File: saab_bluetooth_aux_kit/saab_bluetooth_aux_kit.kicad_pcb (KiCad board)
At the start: 2 copper layers, 3 parts, among them U1 CC3-0505SF-E, U2 ESP32-WROOM-DEVKIT, U4 UDA1334A_BREAKOUT

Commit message: Made simple PCB
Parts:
- added J1: Barrel_Jack, Connector_BarrelJack:BarrelJack_Wuerth_6941xx301002, F.Cu at (133.3, 104.1)
- added U3: MCP2515_MODULE, custom_footprints:MCP2515_Module, F.Cu at (162.6, 116.3)
- U2: value ESP32-WROOM-DEVKIT -> ESP32-WROOM-DEVKIT-custom_symbols
- moved U1 27.8 mm to (134.4, 89.2)
- moved U4 21.0 mm to (161.9, 88.9)
- moved U2 4.59 mm to (110.5, 101.6)
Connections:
- U1 pad 1: (no net) -> Net-(J1-Pad1)
- U1 pad 3: (no net) -> Net-(J1-Pad2)
- U1 pad 5: (no net) -> GND
- U1 pad 7: (no net) -> 5VDC
- U2 pad 3V3: (no net) -> 3VDC
- U2 pad GND: (no net) -> GND
- U2 pad GPIO18: (no net) -> SPI_SCLK
- U2 pad GPIO19: (no net) -> SPI_MISO
- U2 pad GPIO22: (no net) -> I2S_DIN
- U2 pad GPIO23: (no net) -> SPI_MOSI
- U2 pad GPIO25: (no net) -> I2S_WSEL
- U2 pad GPIO26: (no net) -> I2S_BCLK
- U2 pad GPIO5: (no net) -> SPI_CS
- U2 pad VIN: (no net) -> 5VDC
- U4 pad BCLK: (no net) -> I2S_BCLK
- U4 pad DIN: (no net) -> I2S_DIN
- U4 pad GND: (no net) -> GND
- U4 pad SF0: (no net) -> GND
- U4 pad SF1: (no net) -> GND
- U4 pad VIN: (no net) -> 3VDC
- U4 pad WSEL: (no net) -> I2S_WSEL
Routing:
- net GND: track 0.00 -> 131.4 mm
- net 5VDC: track 0.00 -> 97.7 mm
- net I2S_WSEL: track 0.00 -> 90.7 mm
- net I2S_BCLK: track 0.00 -> 83.8 mm
- net 3VDC: track 0.00 -> 54.0 mm
- net SPI_MOSI: track 0.00 -> 48.0 mm
- net I2S_DIN: track 0.00 -> 47.3 mm
- net SPI_MISO: track 0.00 -> 34.8 mm
- net SPI_SCLK: track 0.00 -> 32.5 mm
- net SPI_CS: track 0.00 -> 31.4 mm
- net Net-(J1-Pad2): track 0.00 -> 11.7 mm
- net Net-(J1-Pad1): track 0.00 -> 9.02 mm
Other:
- board outline added: 88.9 x 57.2 mm

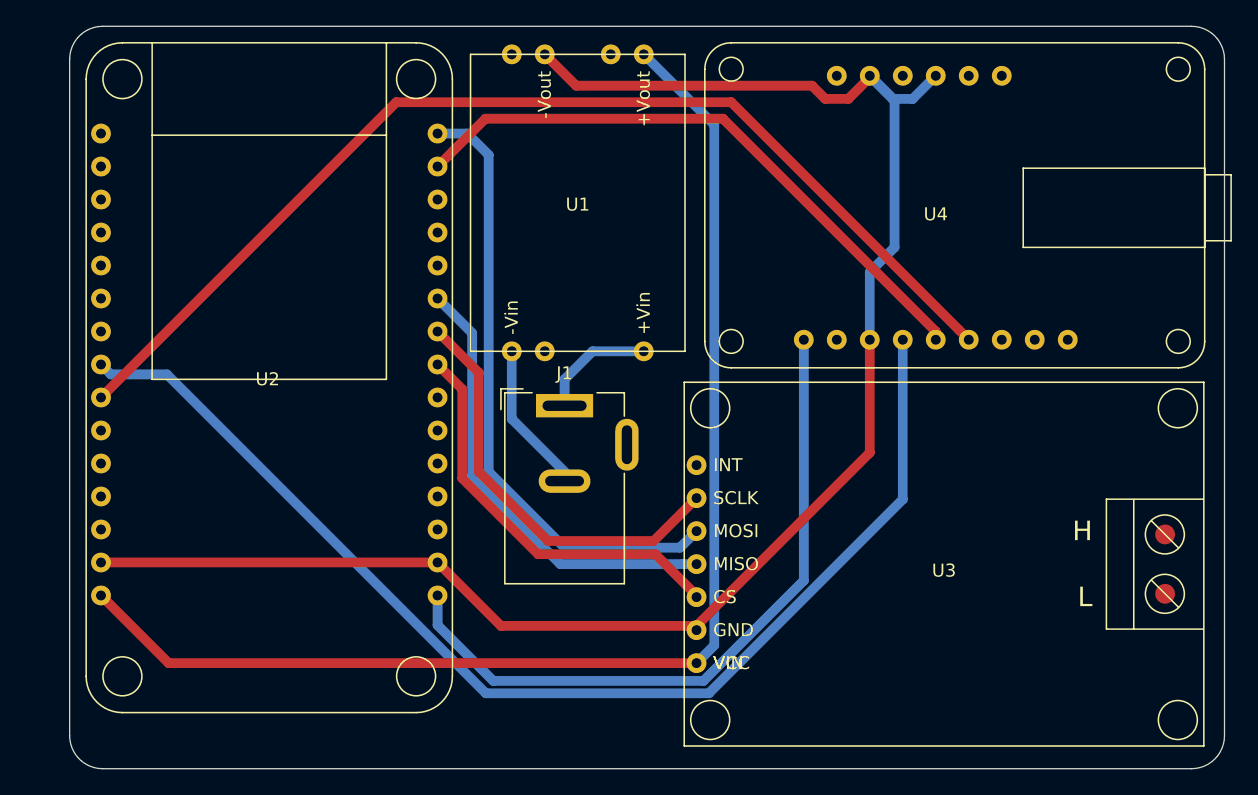
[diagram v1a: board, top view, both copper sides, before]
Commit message: Updated PCB text
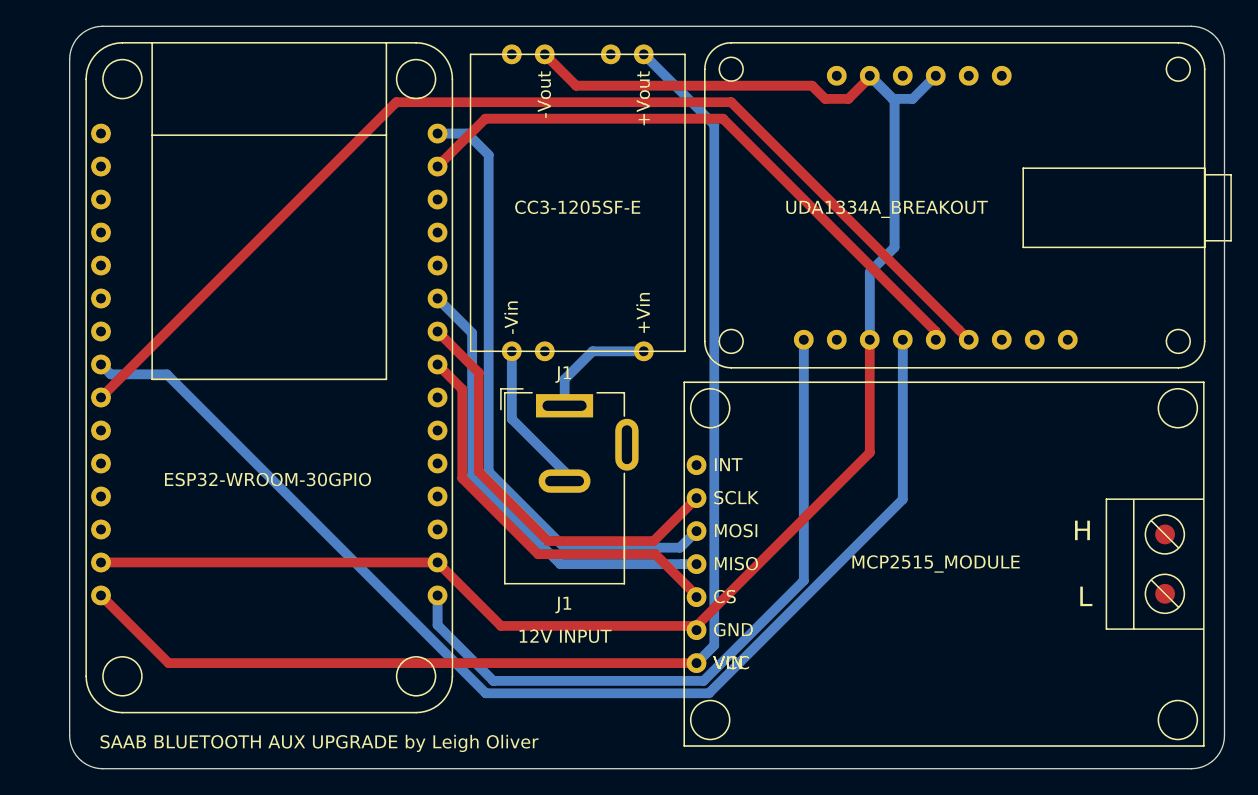
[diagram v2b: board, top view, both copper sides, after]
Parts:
- U1: value CC3-0505SF-E -> CC3-1205SF-E
- U2: value ESP32-WROOM-DEVKIT-custom_symbols -> ESP32-WROOM-30GPIO
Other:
- board text added: "12V INPUT"
- board text added: "SAAB BLUETOOTH AUX UPGRADE by Leigh Oliver"
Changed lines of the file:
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@@
   (general
     (thickness 1.6)
-    (drawings 8)
+    (drawings 10)
     (tracks 71)
     (zones 0)
@@
   )
   (setup
-    (last_trace_width 0.5)
+    (last_trace_width 0.25)
     (user_trace_width 0.5)
     (trace_clearance 0.2)
@@
     (fp_line (start -4.6 13.7) (end -4.6 -1) (layer F.SilkS) (width 0.12))
     (fp_line (start 4.6 13.7) (end -4.6 13.7) (layer F.SilkS) (width 0.12))
-    (fp_text user %R (at 0 7.5) (layer F.Fab)
+    (fp_text user %R (at 0 15.24) (layer F.SilkS)
       (effects (font (size 1 1) (thickness 0.15)))
     )
@@
   (module custom_footprints:MCP2515_Module (layer F.Cu)
     (at 162.56 116.332)
-    (fp_text reference U3 (at 0 0.5) (layer F.SilkS)
-      (effects (font (size 1 1) (thickness 0.15)))
-    )
-    (fp_text value MCP2515_MODULE (at 0 -0.5) (layer F.Fab)
+    (fp_text reference U3 (at 0 0.5) (layer F.SilkS) hide
+      (effects (font (size 1 1) (thickness 0.15)))
+    )
+    (fp_text value MCP2515_MODULE (at -0.635 -0.127) (layer F.SilkS)
       (effects (font (size 1 1) (thickness 0.15)))
     )
@@
   (module custom_footprints:UDA1334A-Breakout (layer F.Cu)
     (at 161.925 88.9)
-    (fp_text reference U4 (at 0 0.5) (layer F.SilkS)
-      (effects (font (size 1 1) (thickness 0.15)))
-    )
-    (fp_text value UDA1334A_BREAKOUT (at 0 -0.5) (layer F.Fab)
+    (fp_text reference U4 (at 0 0.5) (layer F.SilkS) hide
+      (effects (font (size 1 1) (thickness 0.15)))
+    )
+    (fp_text value UDA1334A_BREAKOUT (at -3.81 0) (layer F.SilkS)
       (effects (font (size 1 1) (thickness 0.15)))
     )
@@
   (module custom_footprints:ESP32-WROOM-30GPIO (layer F.Cu)
     (at 110.49 101.6)
-    (fp_text reference U2 (at 0 0.5) (layer F.SilkS)
-      (effects (font (size 1 1) (thickness 0.15)))
-    )
-    (fp_text value ESP32-WROOM-DEVKIT-custom_symbols (at 0 -0.5) (layer F.Fab)
+    (fp_text reference U2 (at 0 0.5) (layer F.SilkS) hide
+      (effects (font (size 1 1) (thickness 0.15)))
+    )
+    (fp_text value ESP32-WROOM-30GPIO (at 0 8.255) (layer F.SilkS)
       (effects (font (size 1 1) (thickness 0.15)))
     )
@@
   (module custom_footprints:CC3-1205SF-E (layer F.Cu)
     (at 134.366 89.154 180)
-    (fp_text reference U1 (at 0 0.5) (layer F.SilkS)
-      (effects (font (size 1 1) (thickness 0.15)))
-    )
-    (fp_text value CC3-0505SF-E (at 0 -0.5) (layer F.Fab)
+    (fp_text reference U1 (at 0 0.5) (layer F.SilkS) hide
+      (effects (font (size 1 1) (thickness 0.15)))
+    )
+    (fp_text value CC3-1205SF-E (at 0 0.254) (layer F.SilkS)
       (effects (font (size 1 1) (thickness 0.15)))
     )
@@
       (net 11 "Net-(J1-Pad1)"))
   )
+  (gr_text "12V INPUT" (at 133.35 121.92) (layer F.SilkS)
+    (effects (font (size 1 1) (thickness 0.15)))
+  )
+  (gr_text "SAAB BLUETOOTH AUX UPGRADE by Leigh Oliver" (at 97.536 130.048) (layer F.SilkS)
+    (effects (font (size 1 1) (thickness 0.15)) (justify left))
+  )
   (gr_arc (start 97.79 129.54) (end 95.25 129.54) (angle -90) (layer Edge.Cuts) (width 0.05))

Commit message: Updated CAN connector pads
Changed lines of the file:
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@@
     (mod_text_width 0.15)
     (pad_size 1.524 1.524)
-    (pad_drill 0.762)
+    (pad_drill 0)
     (pad_to_mask_clearance 0.051)
     (solder_mask_min_width 0.25)
@@
     (add_net "Net-(J1-Pad1)")
     (add_net "Net-(J1-Pad2)")
+    (add_net "Net-(U1-Pad2)")
+    (add_net "Net-(U1-Pad4)")
+    (add_net "Net-(U1-Pad6)")
+    (add_net "Net-(U2-PadEN)")
+    (add_net "Net-(U2-PadGPIO1)")
+    (add_net "Net-(U2-PadGPIO12)")
+    (add_net "Net-(U2-PadGPIO13)")
+    (add_net "Net-(U2-PadGPIO14)")
+    (add_net "Net-(U2-PadGPIO15)")
+    (add_net "Net-(U2-PadGPIO16)")
+    (add_net "Net-(U2-PadGPIO17)")
+    (add_net "Net-(U2-PadGPIO2)")
+    (add_net "Net-(U2-PadGPIO21)")
+    (add_net "Net-(U2-PadGPIO27)")
+    (add_net "Net-(U2-PadGPIO3)")
+    (add_net "Net-(U2-PadGPIO32)")
+    (add_net "Net-(U2-PadGPIO33)")
+    (add_net "Net-(U2-PadGPIO34)")
+    (add_net "Net-(U2-PadGPIO35)")
+    (add_net "Net-(U2-PadGPIO36)")
+    (add_net "Net-(U2-PadGPIO39)")
+    (add_net "Net-(U2-PadGPIO4)")
+    (add_net "Net-(U3-PadCANH)")
+    (add_net "Net-(U3-PadCANL)")
+    (add_net "Net-(U3-PadINT)")
+    (add_net "Net-(U4-Pad3V0)")
+    (add_net "Net-(U4-PadAGND)")
+    (add_net "Net-(U4-PadDEEM)")
+    (add_net "Net-(U4-PadLout)")
+    (add_net "Net-(U4-PadMUTE)")
+    (add_net "Net-(U4-PadPLL)")
+    (add_net "Net-(U4-PadRout)")
+    (add_net "Net-(U4-PadSCLK)")
     (add_net SPI_CS)
     (add_net SPI_MISO)
@@
       (effects (font (size 1 1) (thickness 0.15)) (justify left))
     )
-    (pad CANL connect circle (at 17.018 2.286) (size 1.524 1.524) (layers F.Cu F.Mask))
-    (pad CANH connect circle (at 17.018 -2.286) (size 1.524 1.524) (layers F.Cu F.Mask))
+    (pad CANL connect circle (at 17.018 2.286) (size 1.524 1.524) (layers F.SilkS))
+    (pad CANH connect circle (at 17.018 -2.286) (size 1.524 1.524) (layers F.SilkS))
     (pad VIN thru_hole circle (at -19.05 7.62) (size 1.524 1.524) (drill 0.762) (layers *.Cu *.Mask)
       (net 2 5VDC))

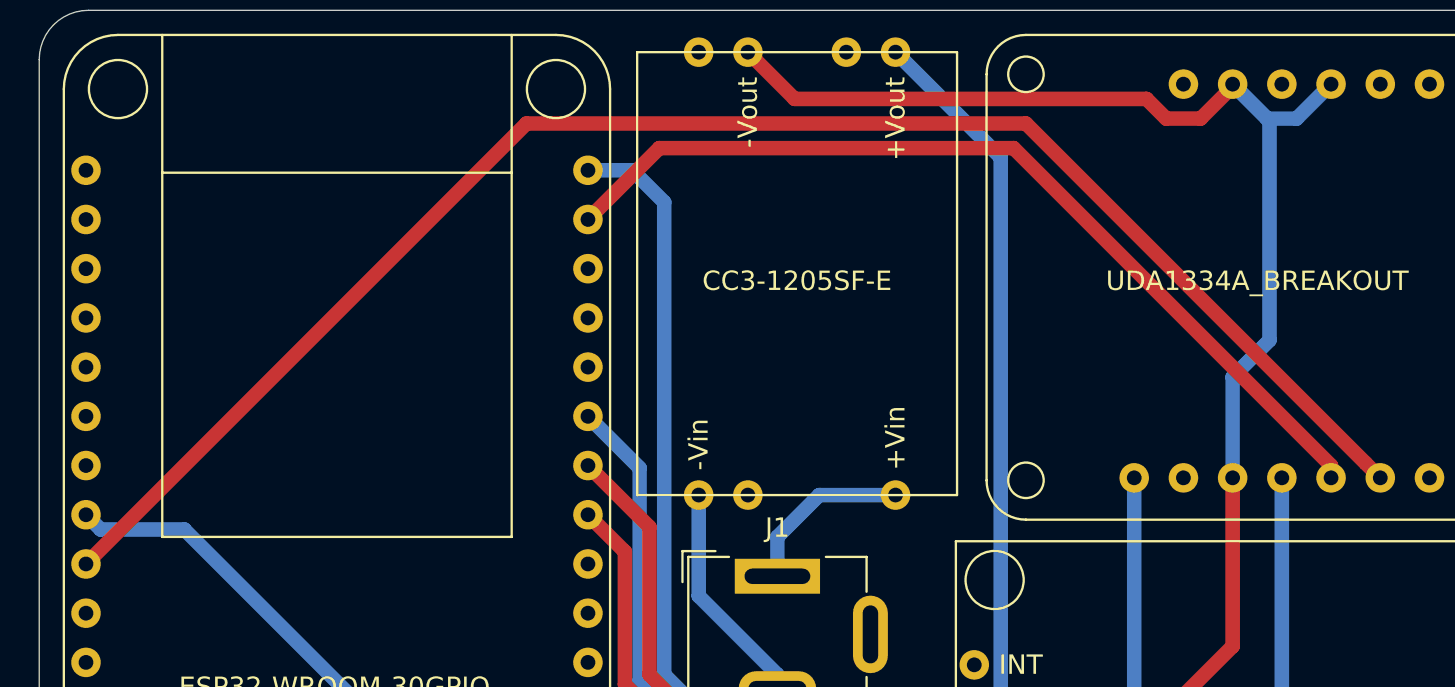
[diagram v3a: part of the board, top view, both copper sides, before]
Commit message: Sent off first prototype board to the fab house
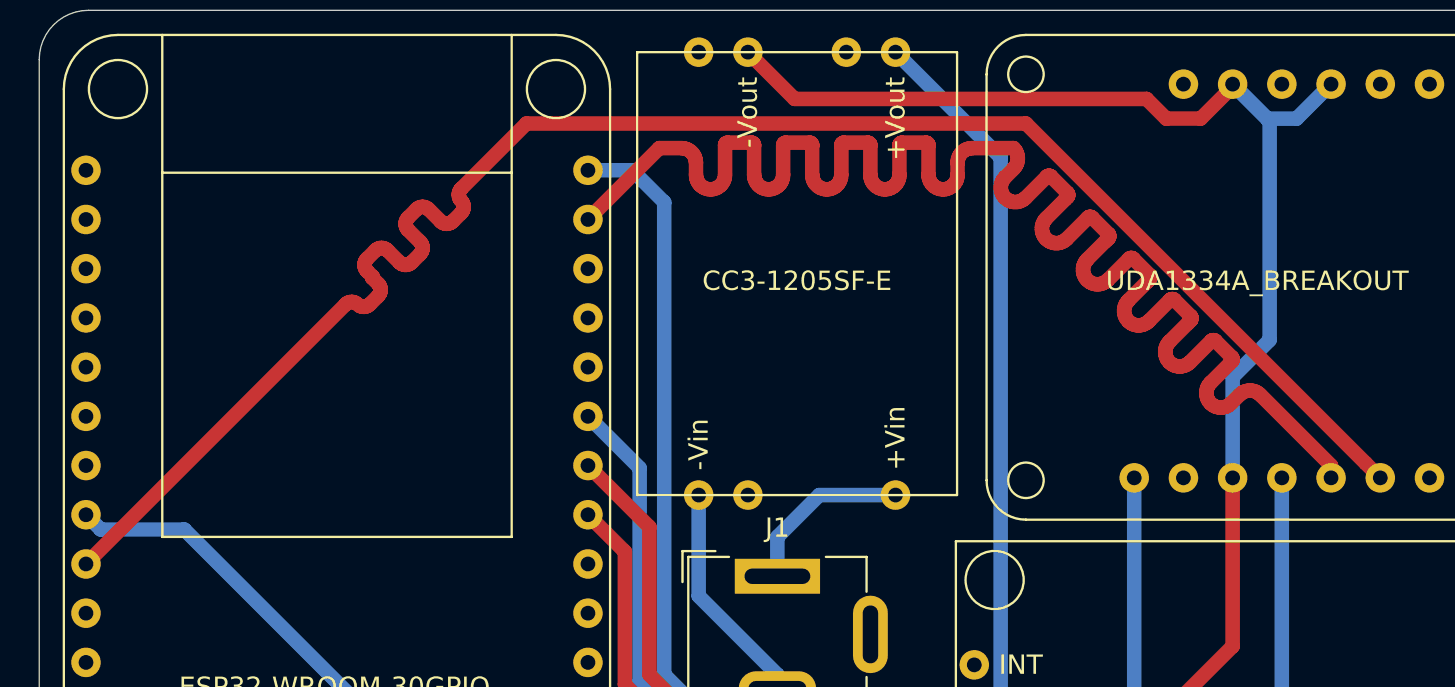
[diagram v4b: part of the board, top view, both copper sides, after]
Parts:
- added G***: LOGO, custom_footprints:saab_logo, B.Cu at (168.9, 116.8)
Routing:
- net I2S_DIN: track 47.3 -> 90.1 mm
- net I2S_BCLK: track 83.8 -> 90.3 mm

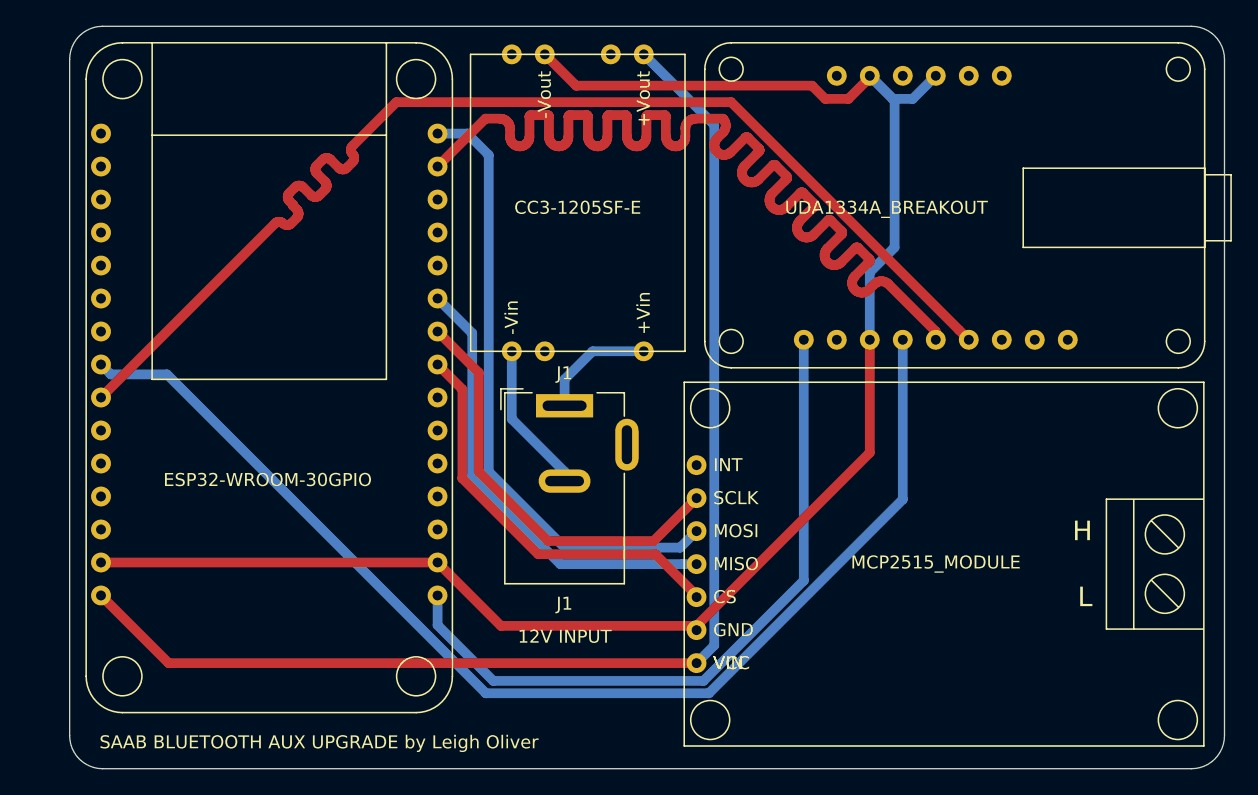
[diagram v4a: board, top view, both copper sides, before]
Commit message: Fixed CC3 DC-DC module footprint orientation. It was flipped. Tied enable pin to gnd. Re-routed I2C data.
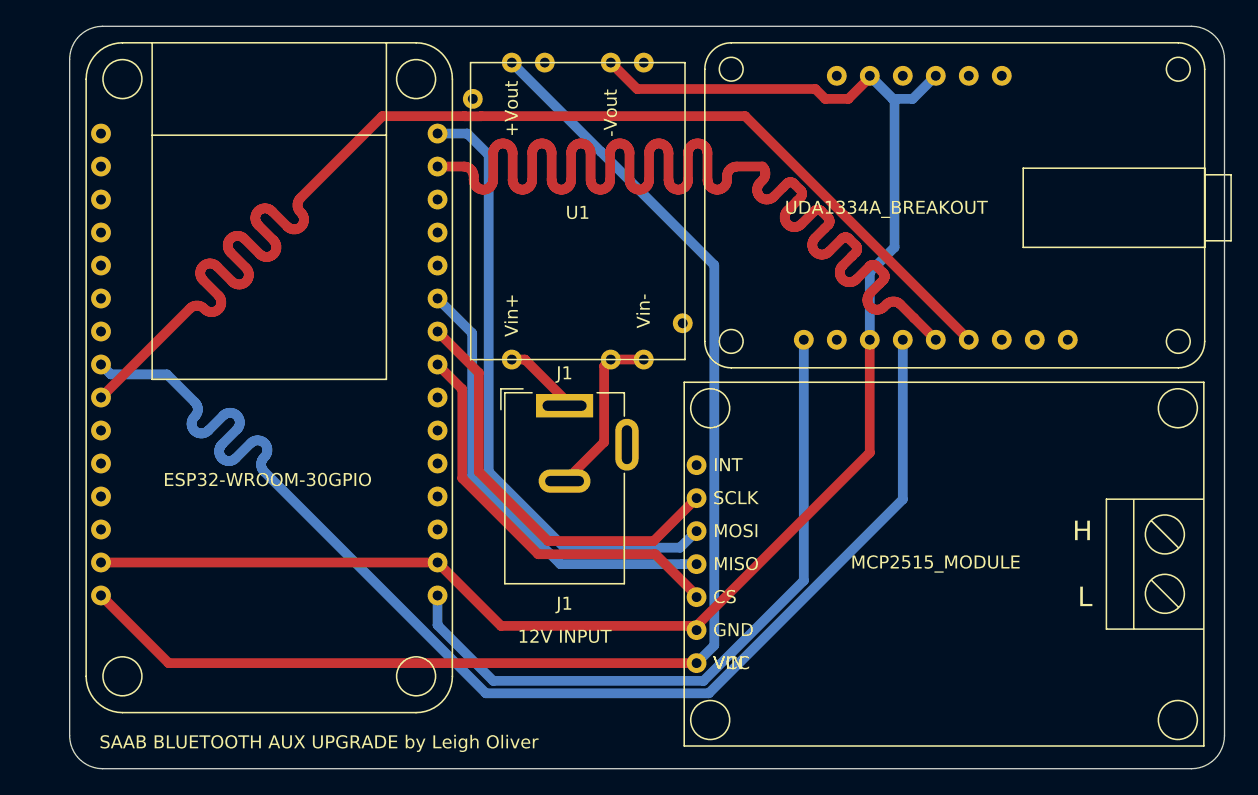
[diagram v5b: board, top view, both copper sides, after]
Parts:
- removed G***: LOGO, custom_footprints:saab_logo
- turned U1 to 0 degrees
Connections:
- U1 pad 2: (no net) -> Net-(J1-Pad2)
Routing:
- net I2S_DIN: track 90.1 -> 100.0 mm
- net I2S_BCLK: track 90.3 -> 100.0 mm
- net I2S_WSEL: track 90.7 -> 100.0 mm
- net GND: track 131.4 -> 126.1 mm
- net 5VDC: track 97.7 -> 101.3 mm
- net Net-(J1-Pad1): track 9.02 -> 5.83 mm
- net Net-(J1-Pad2): track 11.7 -> 13.4 mm
